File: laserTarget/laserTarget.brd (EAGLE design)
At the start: 25.4 x 25.4 mm, 13 parts, among them Q1 MOSFET-NCHANNELBSS123LT1G, Q2 2n3904, U1 red

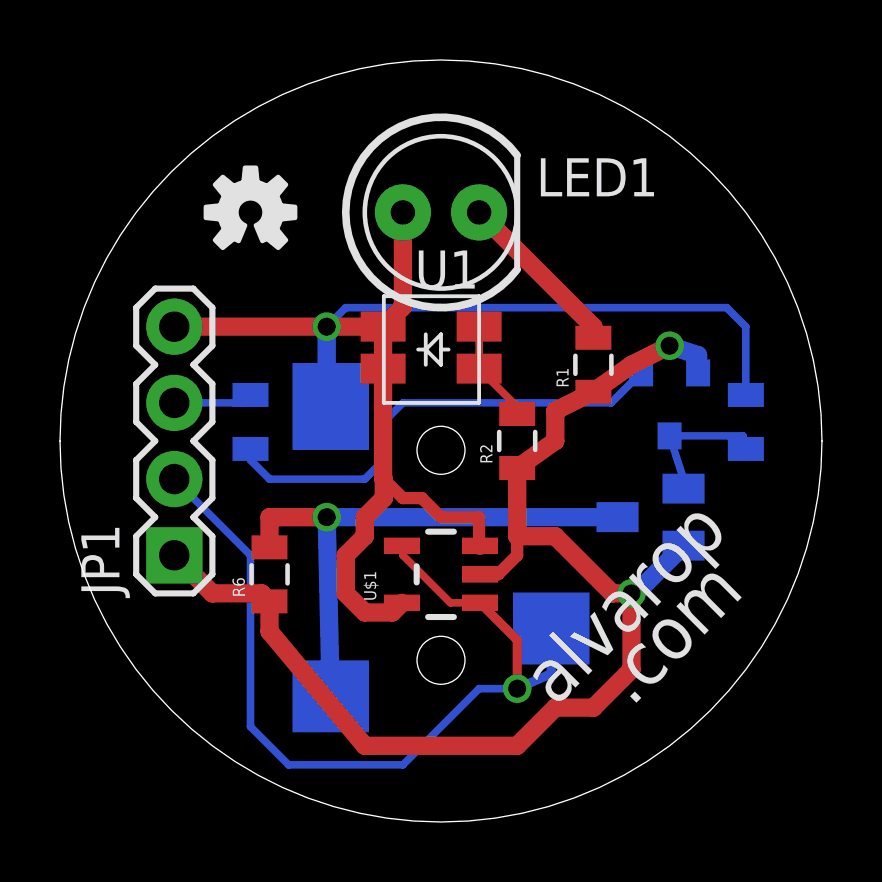
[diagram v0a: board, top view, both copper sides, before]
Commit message: Stupid. Sensor output not connected (was connected to 5V instead...)
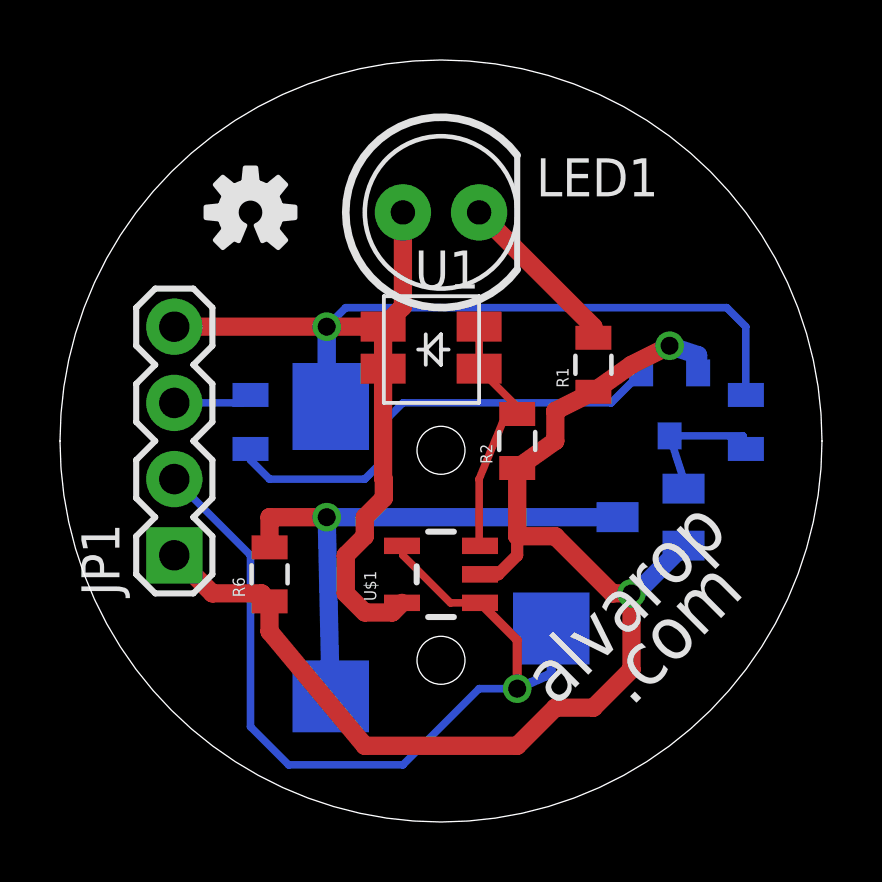
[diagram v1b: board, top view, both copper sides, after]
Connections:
- net 5V: no longer U$1.3
- net N$1: now also U$1.3
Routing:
- net N$1: track 3.44 -> 8.39 mm
- net 5V: track 46.9 -> 42.2 mm
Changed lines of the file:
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@@
 <wire x1="13.97" y1="15.11" x2="15.24" y2="13.84" width="0.254" layer="1"/>
 <wire x1="15.24" y1="13.84" x2="15.24" y2="13.6" width="0.254" layer="1"/>
+<contactref element="U$1" pad="3"/>
+<wire x1="15.24" y1="13.6" x2="14.87" y2="13.6" width="0.254" layer="1"/>
+<wire x1="14.87" y1="13.6" x2="13.97" y2="11.43" width="0.254" layer="1"/>
+<wire x1="13.97" y1="11.43" x2="13.97" y2="9.2351" width="0.254" layer="1"/>
+<wire x1="13.97" y1="9.2351" x2="14.0001" y2="9.205" width="0.254" layer="1"/>
 </signal>
 <signal name="5V">
@@
 <contactref element="LED1" pad="A"/>
 <contactref element="U$1" pad="5"/>
-<contactref element="U$1" pad="3"/>
 <contactref element="U$2" pad="P$2"/>
 <contactref element="R4" pad="2"/>
@@
 <via x="8.89" y="16.51" extent="1-16" drill="0.6"/>
 <wire x1="8.89" y1="16.51" x2="10.77" y2="16.51" width="0.6096" layer="1"/>
-<wire x1="13.97" y1="10.16" x2="12.7" y2="10.16" width="0.4064" layer="1"/>
-<wire x1="12.7" y1="10.16" x2="12.065" y2="10.795" width="0.4064" layer="1"/>
-<wire x1="12.065" y1="10.795" x2="11.43" y2="10.795" width="0.4064" layer="1"/>
-<wire x1="11.43" y1="10.795" x2="10.795" y2="11.43" width="0.4064" layer="1"/>
 <wire x1="10.795" y1="11.43" x2="10.77" y2="11.455" width="0.4064" layer="1"/>
 <wire x1="10.77" y1="11.455" x2="10.77" y2="15.11" width="0.6096" layer="1"/>
@@
 <wire x1="22.225" y1="17.145" x2="9.525" y2="17.145" width="0.254" layer="16"/>
 <wire x1="9.525" y1="17.145" x2="8.89" y2="16.51" width="0.254" layer="16"/>
-<wire x1="14.0001" y1="9.205" x2="13.97" y2="9.2351" width="0.6096" layer="1"/>
-<wire x1="13.97" y1="9.2351" x2="13.97" y2="10.16" width="0.4064" layer="1"/>
 <wire x1="11.3999" y1="7.305" x2="11.0799" y2="6.985" width="0.6096" layer="1"/>
 <wire x1="11.0799" y1="6.985" x2="10.16" y2="6.985" width="0.6096" layer="1"/>

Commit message: Removed test stuff from target
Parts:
- removed JP1: (no value), SparkFun-Connectors:1X04
- removed Q1: MOSFET-NCHANNELBSS123LT1G, SparkFun-DiscreteSemi:SOT23
- removed Q2: 2n3904, SparkFun-DiscreteSemi:SOT23-3
- removed R3: 1k, SparkFun-Resistors:0805
- removed R4: 1M, SparkFun-Resistors:0805
- removed R6: 0, SparkFun-Resistors:0805
- flipped LOGO1 to the bottom
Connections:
- removed net N$3: JP1.3, R3.1
- removed net N$4: Q2.1, R3.2
- removed net N3: Q1.1, Q2.3, R4.1
- removed net TGTGND: Q1.3, R6.2, U$2.P$3
- net 5V: no longer JP1.4, R4.2
- net GND: now also U$2.P$3; no longer JP1.1, Q1.2, Q2.2, R6.1
- net VSENSE: no longer JP1.2
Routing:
- net GND: track 42.2 -> 13.6 mm, vias 2 -> 1
- net TGTGND: track 18.6 -> 0.00 mm, vias 1 -> 0
- net VSENSE: track 29.4 -> 11.7 mm
- net N$4: track 15.9 -> 0.00 mm
- net 5V: track 42.2 -> 27.6 mm
- net N3: track 4.72 -> 0.00 mm
- net N$1: track 8.39 -> 12.3 mm
- net N$3: track 2.65 -> 0.00 mm
- added copper zone on layer 1, net GND
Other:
- board text added: "Target"
- board text added: "v1.1"
